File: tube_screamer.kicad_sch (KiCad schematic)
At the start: 46 parts, among them Q1 MMBT5551, Q2 MMBT5551, Q3 MMBT5551, U1 NE5532

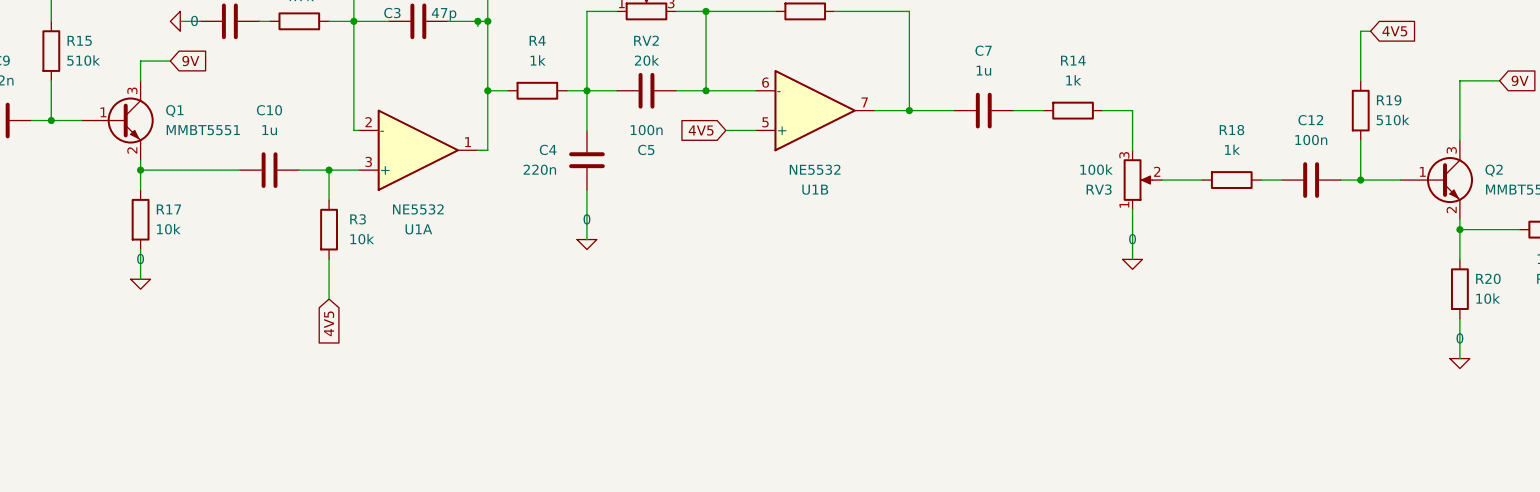
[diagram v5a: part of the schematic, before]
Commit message: Added switch connectors.
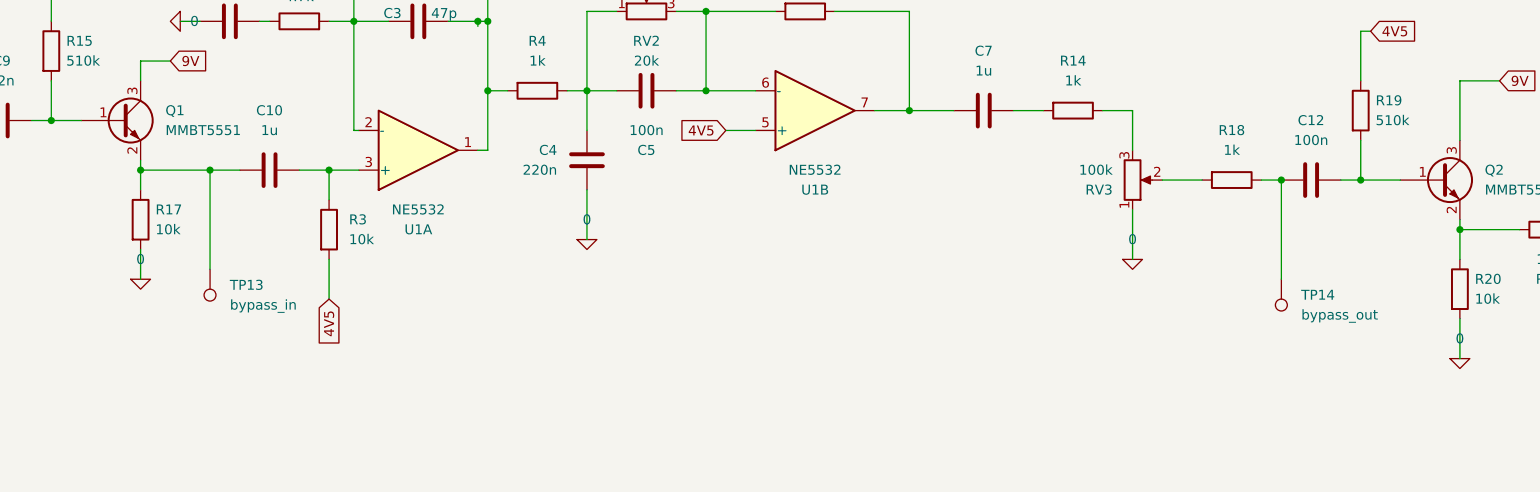
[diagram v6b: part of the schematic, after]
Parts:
- added TP13: bypass_in, TestPoint:TestPoint_THTPad_2.5x2.5mm_Drill1.2mm, symbol Connector:TestPoint
- added TP14: bypass_out, TestPoint:TestPoint_THTPad_2.5x2.5mm_Drill1.2mm, symbol Connector:TestPoint
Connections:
- net at C10.1, Q1.2 (E), R17.1: now also TP13.1
- net at C12.1, R18.1: now also TP14.1
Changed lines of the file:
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@@
 	)
 	(junction
+		(at 74.93 68.58)
+		(diameter 0)
+		(color 0 0 0 0)
+	)
+	(junction
 		(at 234.95 76.2)
 		(diameter 0)
@@
 	)
 	(junction
+		(at 212.09 69.85)
+		(diameter 0)
+		(color 0 0 0 0)
+	)
+	(junction
 		(at 121.92 163.195)
 		(diameter 0)
@@
 	(wire
 		(pts
+			(xy 74.93 81.28) (xy 74.93 68.58)
+		)
+		(stroke
+			(width 0)
+			(type default)
+		)
+	)
+	(wire
+		(pts
 			(xy 97.79 39.37) (xy 93.345 39.37)
 		)
@@
 	(wire
 		(pts
+			(xy 212.09 82.55) (xy 212.09 69.85)
+		)
+		(stroke
+			(width 0)
+			(type default)
+		)
+	)
+	(wire
+		(pts
 			(xy 85.09 156.21) (xy 73.66 156.21)
 		)
@@
 	(wire
 		(pts
-			(xy 66.04 68.58) (xy 78.74 68.58)
+			(xy 66.04 68.58) (xy 74.93 68.58)
 		)
 		(stroke
@@
 	(wire
 		(pts
+			(xy 74.93 68.58) (xy 78.74 68.58)
+		)
+		(stroke
+			(width 0)
+			(type default)
+		)
+	)
+	(wire
+		(pts
 			(xy 54.61 166.37) (xy 48.26 166.37)
 		)
@@
 	)
 	(symbol
+		(lib_id "Connector:TestPoint")
+		(at 74.93 81.28 180)
+		(unit 1)
+		(exclude_from_sim no)
+		(in_bom yes)
+		(on_board yes)
+		(dnp no)
+		(fields_autoplaced yes)
+		(property "Reference" "TP13"
+			(at 77.47 83.3119 0)
+			(effects
+				(font
+					(size 1.27 1.27)
+				)
+				(justify right)
+			)
+		)
+		(property "Value" "bypass_in"
+			(at 77.47 85.8519 0)
+			(effects
+				(font
+					(size 1.27 1.27)
+				)
+				(justify right)
+			)
+		)
+		(property "Footprint" "TestPoint:TestPoint_THTPad_2.5x2.5mm_Drill1.2mm"
+			(at 69.85 81.28 0)
+			(effects
+				(font
+					(size 1.27 1.27)
+				)
+				(hide yes)
+			)
+		)
+		(property "Datasheet" "~"
+			(at 69.85 81.28 0)
+			(effects
+				(font
+					(size 1.27 1.27)
+				)
+				(hide yes)
+			)
+		)
+		(property "Description" ""
+			(at 74.93 81.28 0)
+			(effects
+				(font
+					(size 1.27 1.27)
+				)
+			)
+		)
+		(pin "1"
+		)
+		(instances
+			(project "tube_screamer"
+				(path "/e0801131-6974-42d8-8070-4ed960891aa7"
+					(reference "TP13")
+					(unit 1)
+				)
+			)
+		)
+	)
+	(symbol
 		(lib_id "Device:C")
 		(at 130.81 40.64 180)
@@
 					(unit 1)
 				)
+			)
+		)
+	)
+	(symbol
+		(lib_id "Connector:TestPoint")
+		(at 212.09 82.55 180)
+		(unit 1)
+		(exclude_from_sim no)
+		(in_bom yes)
+		(on_board yes)
+		(dnp no)
+		(fields_autoplaced yes)
+		(property "Reference" "TP14"
+			(at 214.63 84.5819 0)
+			(effects
+				(font
+					(size 1.27 1.27)
+				)
+				(justify right)
+			)
+		)
+		(property "Value" "bypass_out"
+			(at 214.63 87.1219 0)
+			(effects
+				(font
+					(size 1.27 1.27)
+				)
+				(justify right)
+			)
+		)
+		(property "Footprint" "TestPoint:TestPoint_THTPad_2.5x2.5mm_Drill1.2mm"
+			(at 207.01 82.55 0)
+			(effects
+				(font
+					(size 1.27 1.27)
+				)
+				(hide yes)
+			)
+		)
+		(property "Datasheet" "~"
+			(at 207.01 82.55 0)
+			(effects
+				(font
+					(size 1.27 1.27)
+				)
+				(hide yes)
+			)
+		)
+		(property "Description" ""
+			(at 212.09 82.55 0)
+			(effects
+				(font
+					(size 1.27 1.27)
+				)
+			)
+		)
+		(pin "1"
+		)
+		(instances
+			(project "tube_screamer"
+				(path "/e0801131-6974-42d8-8070-4ed960891aa7"
+					(reference "TP14")
+					(unit 1)
+				)

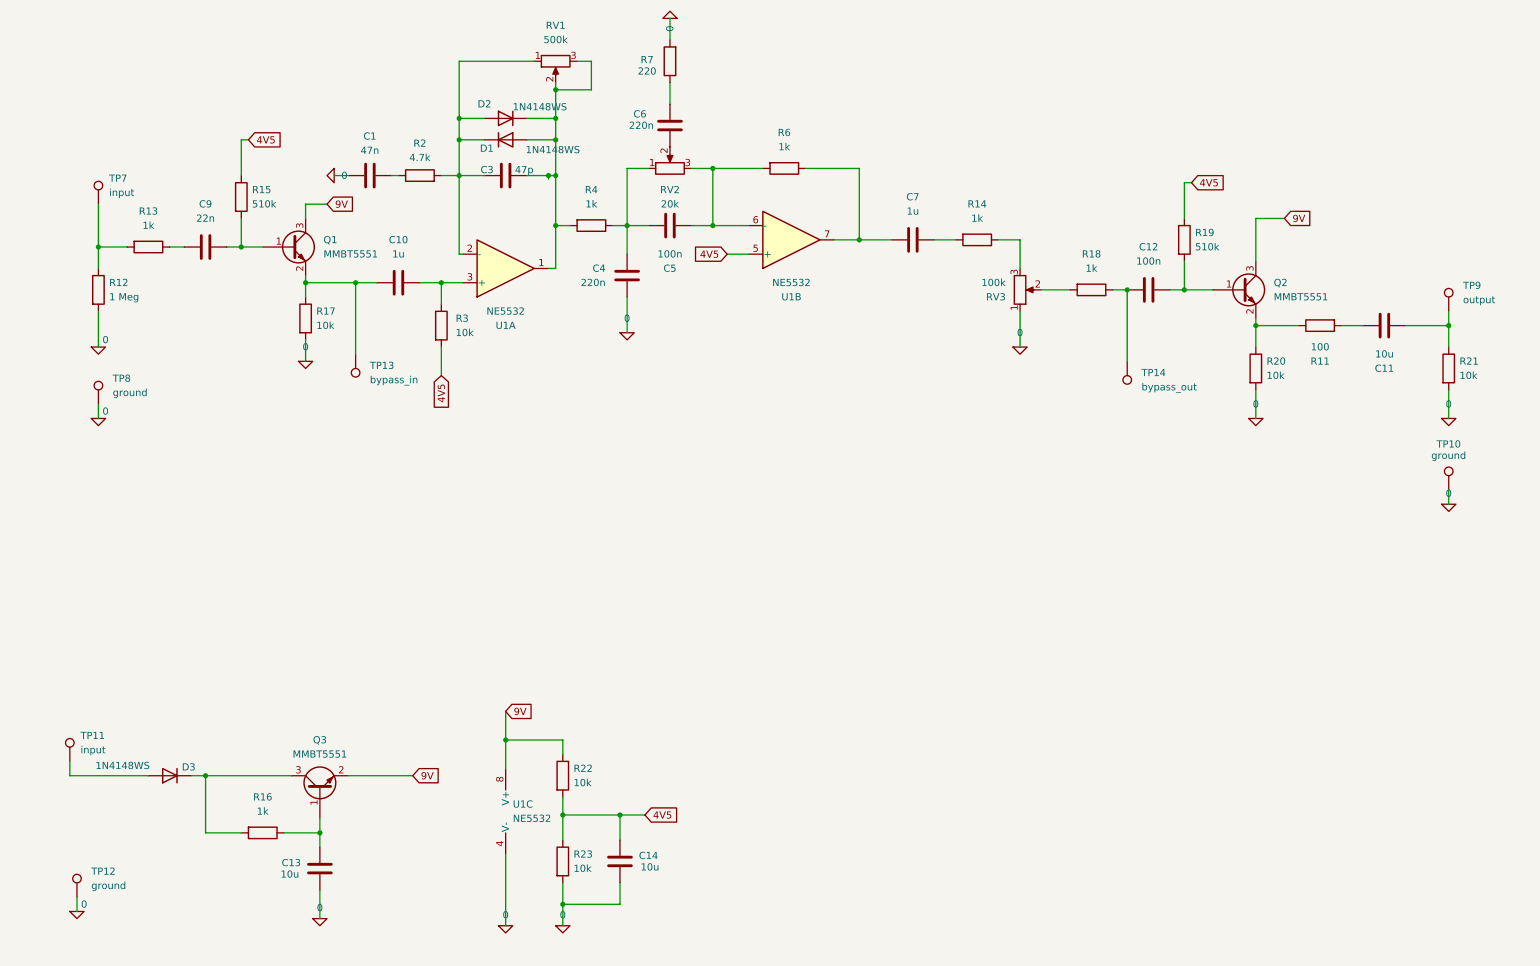
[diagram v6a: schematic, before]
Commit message: Updated switch, added diode.
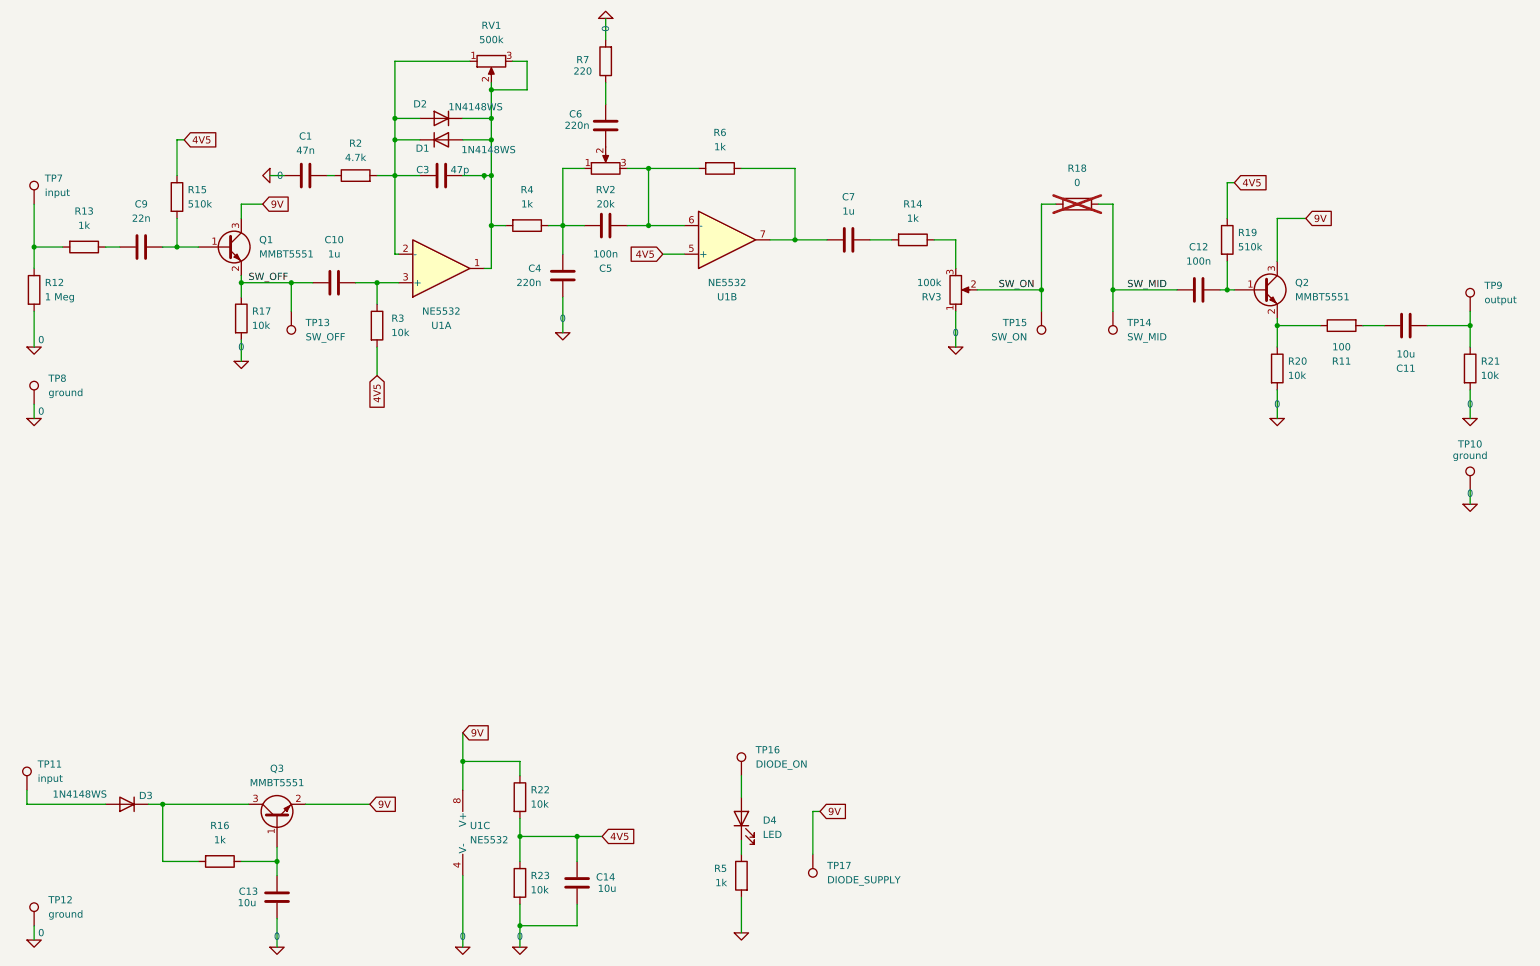
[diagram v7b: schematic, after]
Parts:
- added D4: LED, LED_THT:LED_D5.0mm, symbol Device:LED
- added R5: 1k, Resistor_SMD:R_0603_1608Metric_Pad0.98x0.95mm_HandSolder, symbol Device:R
- added TP15: SW_ON, TestPoint:TestPoint_THTPad_2.5x2.5mm_Drill1.2mm, symbol Connector:TestPoint
- added TP16: DIODE_ON, TestPoint:TestPoint_THTPad_2.5x2.5mm_Drill1.2mm, symbol Connector:TestPoint
- added TP17: DIODE_SUPPLY, TestPoint:TestPoint_THTPad_2.5x2.5mm_Drill1.2mm, symbol Connector:TestPoint
- R18: value 1k -> 0; LCSC C21190 -> (none); now not fitted
- TP13: value bypass_in -> SW_OFF
- TP14: value bypass_out -> SW_MID
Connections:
- net 0: now also R5.2
- net 9V: now also TP17.1
- net SW_ON: now reaches R18.2, RV3.2
- net SW_ON: now also TP15.1
- net SW_OFF: now reaches C10.1, Q1.2 (E), R17.1, TP13.1
- net SW_MID: now reaches C12.1, R18.1, TP14.1
- new net: D4.1 (K), R5.1
- new net: D4.2 (A), TP16.1
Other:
- moved on the sheet: C1, C10, C11, C12, C13, C14, C3, C4, C5, C6, C7, C9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

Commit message: Idk
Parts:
- added C15, C16: 10u, Capacitor_SMD:C_0603_1608Metric_Pad1.08x0.95mm_HandSolder, symbol Device:C
- added C17, C18: 100n, Capacitor_SMD:C_0603_1608Metric_Pad1.08x0.95mm_HandSolder, symbol Device:C
- added C2, C8: 470u, Capacitor_THT:CP_Radial_D8.0mm_P3.50mm, symbol Device:C_Polarized_US
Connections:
- net 0: now also C15.2, C16.2, C17.1, C18.1, C2.2, C8.2
- net 9V: now also C15.1, C16.1, C17.2, C2.1
- net at C13.1, Q3.1 (B), R16.1: now also C18.2, C8.1
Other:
- moved on the sheet: C13, C14, D4, Q3, R16, R22, R23, R5, TP11, TP16, TP17, U1C
